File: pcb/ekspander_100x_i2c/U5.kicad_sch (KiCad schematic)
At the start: 4 parts, among them J12 DG127A-5.08-06P-14-00AH, J13 DG127A-5.08-06P-14-00AH, J14 DG127A-5.08-06P-14-00AH, U5 MCP23017_SP

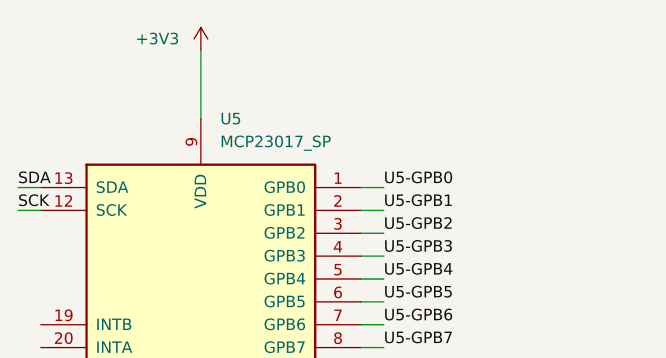
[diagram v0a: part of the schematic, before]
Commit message: Ekspander U2 - U3 - U4 update
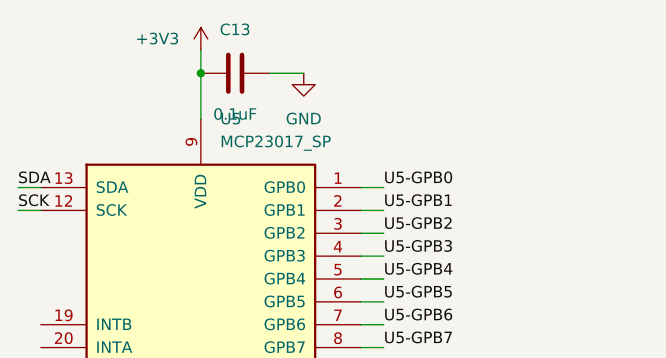
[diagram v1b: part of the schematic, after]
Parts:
- added C13: 0.1uF, Capacitor_SMD:C_0805_2012Metric_Pad1.18x1.45mm_HandSolder, symbol Device:C
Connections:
- net +3V3: now also C13.1
- net GND: now also C13.2
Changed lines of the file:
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@@
 	(generator_version "9.0")
 	(paper "A4")
+	(junction
+		(at 49.53 25.4)
+		(diameter 0)
+		(color 0 0 0 0)
+	)
 	(wire
 		(pts
@@
 	(wire
 		(pts
+			(xy 49.53 25.4) (xy 49.53 30.48)
+		)
+		(stroke
+			(width 0)
+			(type default)
+		)
+	)
+	(wire
+		(pts
 			(xy 69.85 60.96) (xy 67.31 60.96)
 		)
@@
 	(wire
 		(pts
+			(xy 60.96 25.4) (xy 57.15 25.4)
+		)
+		(stroke
+			(width 0)
+			(type default)
+		)
+	)
+	(wire
+		(pts
 			(xy 69.85 78.74) (xy 67.31 78.74)
 		)
@@
 	(wire
 		(pts
-			(xy 49.53 22.86) (xy 49.53 30.48)
+			(xy 49.53 22.86) (xy 49.53 25.4)
 		)
 		(stroke
@@
 				)
 				(justify left)
+			)
+		)
+	)
+	(symbol
+		(lib_id "power:GND")
+		(at 60.96 25.4 0)
+		(unit 1)
+		(exclude_from_sim no)
+		(in_bom yes)
+		(on_board yes)
+		(dnp no)
+		(fields_autoplaced yes)
+		(property "Reference" "#PWR040"
+			(at 60.96 31.75 0)
+			(effects
+				(font
+					(size 1.27 1.27)
+				)
+				(hide yes)
+			)
+		)
+		(property "Value" "GND"
+			(at 60.96 30.48 0)
+			(effects
+				(font
+					(size 1.27 1.27)
+				)
+			)
+		)
+		(property "Footprint" ""
+			(at 60.96 25.4 0)
+			(effects
+				(font
+					(size 1.27 1.27)
+				)
+				(hide yes)
+			)
+		)
+		(property "Datasheet" ""
+			(at 60.96 25.4 0)
+			(effects
+				(font
+					(size 1.27 1.27)
+				)
+				(hide yes)
+			)
+		)
+		(property "Description" "Power symbol creates a global label with name \"GND\" , ground"
+			(at 60.96 25.4 0)
+			(effects
+				(font
+					(size 1.27 1.27)
+				)
+				(hide yes)
+			)
+		)
+		(pin "1"
+		)
+		(instances
+			(project "ekspander_100x_i2c"
+				(path "/824ceec5-564f-405b-8bea-e5a9f7aa2926/89399d0f-8527-42f7-9857-a43fca03c974"
+					(reference "#PWR040")
+					(unit 1)
+				)
 			)
 		)
@@
 					(unit 1)
 				)
+			)
+		)
+	)
+	(symbol
+		(lib_id "Device:C")
+		(at 53.34 25.4 90)
+		(unit 1)
+		(exclude_from_sim no)
+		(in_bom yes)
+		(on_board yes)
+		(dnp no)
+		(property "Reference" "C13"
+			(at 53.34 20.574 90)
+			(effects
+				(font
+					(size 1.27 1.27)
+				)
+			)
+		)
+		(property "Value" "0.1uF"
+			(at 53.34 29.972 90)
+			(effects
+				(font
+					(size 1.27 1.27)
+				)
+			)
+		)
+		(property "Footprint" "Capacitor_SMD:C_0805_2012Metric_Pad1.18x1.45mm_HandSolder"
+			(at 57.15 24.4348 0)
+			(effects
+				(font
+					(size 1.27 1.27)
+				)
+				(hide yes)
+			)
+		)
+		(property "Datasheet" "~"
+			(at 53.34 25.4 0)
+			(effects
+				(font
+					(size 1.27 1.27)
+				)
+				(hide yes)
+			)
+		)
+		(property "Description" "Unpolarized capacitor"
+			(at 53.34 25.4 0)
+			(effects
+				(font
+					(size 1.27 1.27)
+				)
+				(hide yes)
+			)
+		)
+		(pin "2"
+		)
+		(pin "1"
+		)
+		(instances
+			(project "ekspander_100x_i2c"
+				(path "/824ceec5-564f-405b-8bea-e5a9f7aa2926/89399d0f-8527-42f7-9857-a43fca03c974"
+					(reference "C13")
+					(unit 1)
+				)

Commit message: Ekspander U5 - U6 update
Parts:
- added C23, C24: 0.1uF, Capacitor_SMD:C_0805_2012Metric_Pad1.18x1.45mm_HandSolder, symbol Device:C
- added U26, U29: LTV-847, Package_DIP:DIP-16_W7.62mm, symbol Isolator:LTV-847
- added U27, U28: ITS716G, Package_SO:SOIC-20W_7.5x12.8mm_P1.27mm, symbol Driver_FET:ITS716G
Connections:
- net GND: now also C23.2, C24.2, U26.11, U26.13, U26.15, U26.2, U26.4, U26.6, U26.8, U26.9, U27.2 (GND1/2), U27.6 (GND3/4), U28.2 (GND1/2), U28.6 (GND3/4), U29.11, U29.13, U29.15, U29.2, U29.4, U29.6, U29.8, U29.9
- net U5-GPA0: now also U29.10
- net U5-GPA1: now also U29.12
- net U5-GPA2: now also U29.14
- net U5-GPA3: now also U29.16
- net U5-GPA4: now also U28.9 (IN4)
- net U5-GPA5: now also U28.7 (IN3)
- net U5-GPA6: now also U28.5 (IN2)
- net U5-GPA7: now also U28.3 (IN1)
- net U5-GPB0: now also U26.16
- net U5-GPB1: now also U26.14
- net U5-GPB2: now also U26.12
- net U5-GPB3: now also U26.10
- net U5-GPB4: now also U27.3 (IN1)
- net U5-GPB5: now also U27.5 (IN2)
- net U5-GPB6: now also U27.7 (IN3)
- net U5-GPB7: now also U27.9 (IN4)
- net ZC74_CLOSE_LED: now reaches J12.1
- net ZC74_CLOSE_LED: now also U26.5
- net ZC74_OPEN_LED: now reaches J12.2
- net ZC74_OPEN_LED: now also U26.7
- net ZC72_CLOSE_MOTOR: now reaches J12.3
- net ZC72_OPEN_MOTOR: now reaches J12.4
- net ZC71_CLOSE_MOTOR: now reaches J12.5
- net ZC71_OPEN_MOTOR: now reaches J12.6
- net ZC75_OPEN_MOTOR: now reaches J14.1
- net ZC75_OPEN_MOTOR: now also U28.18 (OUT1)
- net ZC75_CLOSE_MOTOR: now reaches J14.2
- net ZC75_CLOSE_MOTOR: now also U28.17 (OUT2)
- net ZC76_OPEN_LED: now reaches J14.3
- net ZC76_OPEN_LED: now also U29.7
- net ZC76_CLOSE_LED: now reaches J14.4
- net ZC76_CLOSE_LED: now also U29.5
- net ZC75_CLOSE_LED: now reaches J14.5
- net ZC75_CLOSE_LED: now also U29.3
- net ZC75_OPEN_LED: now reaches J14.6
- net ZC75_OPEN_LED: now also U29.1
- net ZC74_CLOSE_MOTOR: now reaches J13.1
- net ZC74_CLOSE_MOTOR: now also U27.13 (OUT4)
- net ZC74_OPEN_MOTOR: now reaches J13.2
- net ZC74_OPEN_MOTOR: now also U27.14 (OUT3)
- net ZC73_CLOSE_MOTOR: now reaches J13.3
- net ZC73_CLOSE_MOTOR: now also U27.17 (OUT2)
- net ZC73_OPEN_MOTOR: now reaches J13.4
- net ZC73_OPEN_MOTOR: now also U27.18 (OUT1)
- net ZC73_CLOSE_LED: now reaches J13.5
- net ZC73_CLOSE_LED: now also U26.3
- net ZC73_OPEN_LED: now reaches J13.6
- net ZC73_OPEN_LED: now also U26.1
- new net +24V: C23.1, C24.1, U27.1 (VBB), U27.10 (VBB), U27.11 (VBB), U27.12 (VBB), U27.15 (VBB), U27.16 (VBB), U27.19 (VBB), U27.20 (VBB), U28.1 (VBB), U28.10 (VBB), U28.11 (VBB), U28.12 (VBB), U28.15 (VBB), U28.16 (VBB), U28.19 (VBB), U28.20 (VBB)
- new net ZC76_CLOSE_MOTOR: U28.13 (OUT4)
- new net ZC76_OPEN_MOTOR: U28.14 (OUT3)
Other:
- moved on the sheet: J12, J13, J14

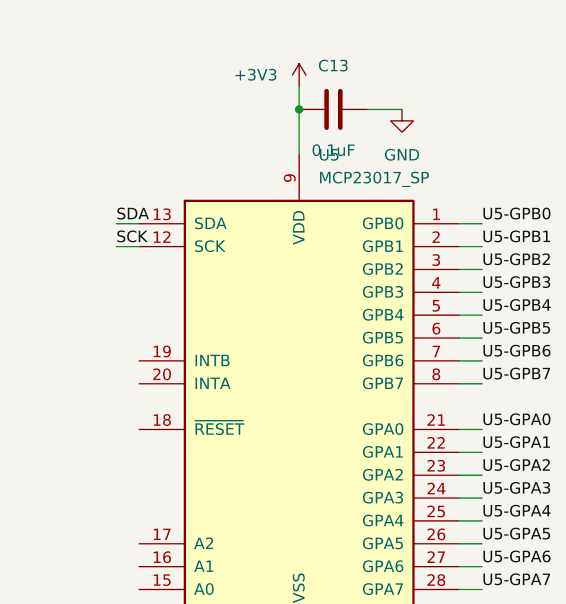
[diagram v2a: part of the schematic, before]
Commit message: Ekspander 24V update
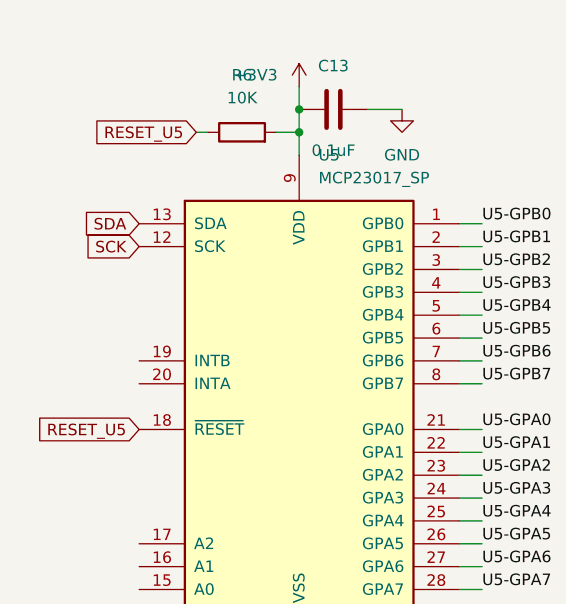
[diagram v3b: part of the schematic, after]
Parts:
- added R6: 10K, PCM_Resistor_SMD_AKL:R_0805_2012Metric_Pad1.20x1.40mm_HandSolder, symbol Device:R
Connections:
- net +3V3: now also R6.2
- net RESET_U5: now reaches U5.18 (~{RESET})
- net RESET_U5: now also R6.1
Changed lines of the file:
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@@
 	(paper "A4")
 	(junction
+		(at 49.53 27.94)
+		(diameter 0)
+		(color 0 0 0 0)
+	)
+	(junction
 		(at 49.53 25.4)
 		(diameter 0)
@@
 	(wire
 		(pts
-			(xy 29.21 40.64) (xy 31.75 40.64)
+			(xy 198.12 119.38) (xy 201.93 119.38)
 		)
 		(stroke
@@
 	(wire
 		(pts
-			(xy 198.12 119.38) (xy 201.93 119.38)
+			(xy 193.04 50.8) (xy 193.04 52.07)
 		)
 		(stroke
@@
 	(wire
 		(pts
-			(xy 193.04 50.8) (xy 193.04 52.07)
+			(xy 46.99 27.94) (xy 49.53 27.94)
 		)
 		(stroke
@@
 	(wire
 		(pts
+			(xy 49.53 27.94) (xy 49.53 30.48)
+		)
+		(stroke
+			(width 0)
+			(type default)
+		)
+	)
+	(wire
+		(pts
 			(xy 251.46 50.8) (xy 251.46 52.07)
 		)
@@
 	(wire
 		(pts
+			(xy 38.1 27.94) (xy 39.37 27.94)
+		)
+		(stroke
+			(width 0)
+			(type default)
+		)
+	)
+	(wire
+		(pts
 			(xy 195.58 21.59) (xy 170.18 21.59)
 		)
@@
 	(wire
 		(pts
-			(xy 29.21 38.1) (xy 31.75 38.1)
-		)
-		(stroke
-			(width 0)
-			(type default)
-		)
-	)
-	(wire
-		(pts
 			(xy 245.11 104.14) (xy 245.11 119.38)
 		)
@@
 	(wire
 		(pts
-			(xy 49.53 25.4) (xy 49.53 30.48)
+			(xy 49.53 25.4) (xy 49.53 27.94)
 		)
 		(stroke
@@
 		)
 	)
-	(label "SCK"
-		(at 29.21 40.64 0)
-		(effects
-			(font
-				(size 1.27 1.27)
-			)
-			(justify left bottom)
-		)
-	)
 	(label "ZC75_OPEN_MOTOR"
 		(at 264.16 30.48 0)
@@
 		)
 	)
-	(label "SDA"
-		(at 29.21 38.1 0)
-		(effects
-			(font
-				(size 1.27 1.27)
-			)
-			(justify left bottom)
-		)
-	)
 	(label "U5-GPB1"
 		(at 205.74 114.3 0)
@@
 		)
 	)
+	(global_label "SCK"
+		(shape input)
+		(at 31.75 40.64 180)
+		(fields_autoplaced yes)
+		(effects
+			(font
+				(size 1.27 1.27)
+			)
+			(justify right)
+		)
+		(property "Intersheetrefs" "${INTERSHEET_REFS}"
+			(at 25.0153 40.64 0)
+			(effects
+				(font
+					(size 1.27 1.27)
+				)
+				(justify right)
+				(hide yes)
+			)
+		)
+	)
 	(global_label "ZC76_CLOSE_LED"
 		(shape input)
@@
 		)
 	)
+	(global_label "RESET_U5"
+		(shape input)
+		(at 38.1 27.94 180)
+		(fields_autoplaced yes)
+		(effects
+			(font
+				(size 1.27 1.27)
+			)
+			(justify right)
+		)
+		(property "Intersheetrefs" "${INTERSHEET_REFS}"
+			(at 25.8621 27.94 0)
+			(effects
+				(font
+					(size 1.27 1.27)
+				)
+				(justify right)
+				(hide yes)
+			)
+		)
+	)
+	(global_label "SDA"
+		(shape input)
+		(at 31.75 38.1 180)
+		(fields_autoplaced yes)
+		(effects
+			(font
+				(size 1.27 1.27)
+			)
+			(justify right)
+		)
+		(property "Intersheetrefs" "${INTERSHEET_REFS}"
+			(at 25.1967 38.1 0)
+			(effects
+				(font
+					(size 1.27 1.27)
+				)
+				(justify right)
+				(hide yes)
+			)
+		)
+	)
 	(global_label "ZC75_CLOSE_LED"
 		(shape input)
@@
 		)
 	)
+	(global_label "RESET_U5"
+		(shape input)
+		(at 31.75 60.96 180)
+		(fields_autoplaced yes)
+		(effects
+			(font
+				(size 1.27 1.27)
+			)
+			(justify right)
+		)
+		(property "Intersheetrefs" "${INTERSHEET_REFS}"
+			(at 19.5121 60.96 0)
+			(effects
+				(font
+					(size 1.27 1.27)
+				)
+				(justify right)
+				(hide yes)
+			)
+		)
+	)
 	(symbol
 		(lib_id "power:GND")
@@
 					(unit 1)
 				)
+			)
+		)
+	)
+	(symbol
+		(lib_id "Device:R")
+		(at 43.18 27.94 90)
+		(unit 1)
+		(exclude_from_sim no)
+		(in_bom yes)
+		(on_board yes)
+		(dnp no)
+		(fields_autoplaced yes)
+		(property "Reference" "R6"
+			(at 43.18 21.59 90)
+			(effects
+				(font
+					(size 1.27 1.27)
+				)
+			)
+		)
+		(property "Value" "10K"
+			(at 43.18 24.13 90)
+			(effects
+				(font
+					(size 1.27 1.27)
+				)
+			)
+		)
+		(property "Footprint" "PCM_Resistor_SMD_AKL:R_0805_2012Metric_Pad1.20x1.40mm_HandSolder"
+			(at 43.18 29.718 90)
+			(effects
+				(font
+					(size 1.27 1.27)
+				)
+				(hide yes)
+			)
+		)
+		(property "Datasheet" "~"
+			(at 43.18 27.94 0)
+			(effects
+				(font
+					(size 1.27 1.27)
+				)
+				(hide yes)
+			)
+		)
+		(property "Description" "Resistor"
+			(at 43.18 27.94 0)
+			(effects
+				(font
+					(size 1.27 1.27)
+				)
+				(hide yes)
+			)
+		)
+		(pin "2"
+		)
+		(pin "1"
+		)
+		(instances
+			(project "ekspander_100x_i2c"
+				(path "/824ceec5-564f-405b-8bea-e5a9f7aa2926/89399d0f-8527-42f7-9857-a43fca03c974"
+					(reference "R6")
+					(unit 1)
+				)
